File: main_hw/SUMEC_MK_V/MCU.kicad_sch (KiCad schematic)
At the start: 7 parts, among them U3 24CW1280T-I/OT, U4 ESP32-S3-WROOM-1

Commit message: plotting + boms
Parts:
- renumbered U3 to Ue
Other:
- note removed: "CHANGE LABELS"
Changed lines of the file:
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@@
 	(text "GPIO  | NAME      | DESC. \n02    | MAIN_BTN  | Schrack light switch; --debounced --pullup \n05    | R_LED     | LEDs, Indication --debug\n06    | G_LED     | LEDs, Indication --debug\n09    | BUZZER    | Passive buzzer\n10    | MISO      | SPI; SD Card\n11    | CLOCK     | SPI clock; SD Card, MAX7219\n12    | MOSI      | SPI; SD Card, MAX7219\n04    | cSelect0  | Chipselect for MAX7219; --defHigh\n13    | cSelect1  | Chipselect for SD Card; --defHigh\n38    | D_EXT1    | External device, eg: LEDs, Button\n39    | D_EXT2    | External device, eg: LEDs, Button\n40    | D_EXT3    | External device, eg: LEDs, Button\n41    | MODE_SW   | External switch, --unused\n42    | RESET_SW  | External switch, Time/Score reset\n\n"
 		(exclude_from_sim no)
-		(at 135.89 139.7 0)
+		(at 139.065 139.7 0)
 		(effects
 			(font
@@
 			)
 			(justify left bottom)
-		)
-	)
-	(text "CHANGE LABELS"
-		(exclude_from_sim no)
-		(at 171.196 43.18 0)
-		(effects
-			(font
-				(size 1.27 1.27)
-			)
 		)
 	)
@@
 	)
 	(no_connect
-		(at 205.74 71.12)
+		(at 208.28 71.12)
 	)
 	(no_connect
-		(at 205.74 73.66)
+		(at 208.28 73.66)
 	)
 	(no_connect
@@
 	(wire
 		(pts
+			(xy 208.28 73.66) (xy 205.74 73.66)
+		)
+		(stroke
+			(width 0)
+			(type default)
+		)
+	)
+	(wire
+		(pts
 			(xy 186.69 40.64) (xy 186.69 46.99)
 		)
@@
 		(pts
 			(xy 92.71 135.89) (xy 93.98 135.89)
+		)
+		(stroke
+			(width 0)
+			(type default)
+		)
+	)
+	(wire
+		(pts
+			(xy 208.28 71.12) (xy 205.74 71.12)
 		)
 		(stroke
@@
 				(justify right)
 				(hide yes)
-			)
-		)
-	)
-	(netclass_flag ""
-		(length 2.54)
-		(shape round)
-		(at 219.71 139.7 0)
-		(fields_autoplaced yes)
-		(effects
-			(font
-				(size 1.27 1.27)
-			)
-			(justify left bottom)
-		)
-		(property "Netclass" "ARES"
-			(at 220.4085 137.16 0)
-			(effects
-				(font
-					(size 1.27 1.27)
-				)
-				(justify left)
-			)
-		)
-		(property "Component Class" "Resistor"
-			(at 220.4085 138.6205 0)
-			(effects
-				(font
-					(size 1.27 1.27)
-					(italic yes)
-				)
-				(justify left)
 			)
 		)
@@
 			)
 		)
+		(property "Sim.Device" ""
+			(at 190.5 78.74 0)
+			(effects
+				(font
+					(size 1.27 1.27)
+				)
+			)
+		)
+		(property "Sim.Pins" ""
+			(at 190.5 78.74 0)
+			(effects
+				(font
+					(size 1.27 1.27)
+				)
+			)
+		)
+		(property "Sim.Type" ""
+			(at 190.5 78.74 0)
+			(effects
+				(font
+					(size 1.27 1.27)
+				)
+			)
+		)
 		(pin "7"
 		)
@@
 		(dnp no)
 		(fields_autoplaced yes)
-		(property "Reference" "U3"
+		(property "Reference" "Ue"
 			(at 96.1741 137.16 0)
 			(effects
@@
 				)
 				(hide yes)
+			)
+		)
+		(property "Sim.Device" ""
+			(at 93.98 147.32 0)
+			(effects
+				(font
+					(size 1.27 1.27)
+				)
+			)
+		)
+		(property "Sim.Pins" ""
+			(at 93.98 147.32 0)
+			(effects
+				(font
+					(size 1.27 1.27)
+				)
+			)
+		)
+		(property "Sim.Type" ""
+			(at 93.98 147.32 0)
+			(effects
+				(font
+					(size 1.27 1.27)
+				)
 			)
 		)
@@
 			(project "SUMEC_MK_V"
 				(path "/900bd7ac-cdf9-4a2f-8b1f-2c21e3760046/7b93d7c5-db1a-415c-92e4-9ebec6cf195f"
-					(reference "U3")
+					(reference "Ue")
 					(unit 1)
 				)
@@
 				)
 				(hide yes)
+			)
+		)
+		(property "Sim.Device" ""
+			(at 222.25 81.28 0)
+			(effects
+				(font
+					(size 1.27 1.27)
+				)
+			)
+		)
+		(property "Sim.Pins" ""
+			(at 222.25 81.28 0)
+			(effects
+				(font
+					(size 1.27 1.27)
+				)
+			)
+		)
+		(property "Sim.Type" ""
+			(at 222.25 81.28 0)
+			(effects
+				(font
+					(size 1.27 1.27)
+				)
 			)
 		)
@@
 			)
 		)
+		(property "Sim.Device" ""
+			(at 88.9 135.89 0)
+			(effects
+				(font
+					(size 1.27 1.27)
+				)
+			)
+		)
+		(property "Sim.Pins" ""
+			(at 88.9 135.89 0)
+			(effects
+				(font
+					(size 1.27 1.27)
+				)
+			)
+		)
+		(property "Sim.Type" ""
+			(at 88.9 135.89 0)
+			(effects
+				(font
+					(size 1.27 1.27)
+				)
+			)
+		)
 		(pin "1"
 		)
@@
 			)
 		)
+		(property "Sim.Device" ""
+			(at 193.04 40.64 0)
+			(effects
+				(font
+					(size 1.27 1.27)
+				)
+			)
+		)
+		(property "Sim.Pins" ""
+			(at 193.04 40.64 0)
+			(effects
+				(font
+					(size 1.27 1.27)
+				)
+			)
+		)
+		(property "Sim.Type" ""
+			(at 193.04 40.64 0)
+			(effects
+				(font
+					(size 1.27 1.27)
+				)
+			)
+		)
 		(pin "1"
 		)
@@
 				)
 				(hide yes)
+			)
+		)
+		(property "Sim.Device" ""
+			(at 229.87 81.28 0)
+			(effects
+				(font
+					(size 1.27 1.27)
+				)
+			)
+		)
+		(property "Sim.Pins" ""
+			(at 229.87 81.28 0)
+			(effects
+				(font
+					(size 1.27 1.27)
+				)
+			)
+		)
+		(property "Sim.Type" ""
+			(at 229.87 81.28 0)
+			(effects
+				(font
+					(size 1.27 1.27)
+				)
 			)
 		)
@@
 			)
 		)
+		(property "Sim.Device" ""
+			(at 193.04 46.99 0)
+			(effects
+				(font
+					(size 1.27 1.27)
+				)
+			)
+		)
+		(property "Sim.Pins" ""
+			(at 193.04 46.99 0)
+			(effects
+				(font
+					(size 1.27 1.27)
+				)
+			)
+		)
+		(property "Sim.Type" ""
+			(at 193.04 46.99 0)
+			(effects
+				(font
+					(size 1.27 1.27)
+				)
+			)
+		)

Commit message: 67yfhtgftu
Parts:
- renumbered Ue to U3
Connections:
- net EN_L: now also U4.7 (IO7); no longer U4.12 (IO8)
- net EN_R: now also U4.12 (IO8); no longer U4.7 (IO7)
- net PH_L: now also U4.6 (IO6); no longer U4.11 (IO18)
- net PH_R: now also U4.11 (IO18); no longer U4.6 (IO6)
- net SHARP_L: now also U4.31 (IO38); no longer U4.18 (IO10)
- net SHARP_R: now also U4.18 (IO10); no longer U4.31 (IO38)
- net BZ_PWM renamed BZ_IO02
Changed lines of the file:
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@@
 		)
 	)
-	(global_label "SHARP_R"
+	(global_label "SHARP_L"
 		(shape input)
 		(at 205.74 81.28 0)
@@
 		)
 		(property "Intersheetrefs" "${INTERSHEET_REFS}"
-			(at 213.9109 81.28 0)
+			(at 213.8005 81.28 0)
 			(effects
 				(font
@@
 		)
 	)
-	(global_label "EN_R"
+	(global_label "EN_L"
 		(shape output)
 		(at 167.64 78.74 180)
@@
 		)
 		(property "Intersheetrefs" "${INTERSHEET_REFS}"
-			(at 162.1264 78.74 0)
-			(effects
-				(font
-					(size 1.27 1.27)
-				)
-				(justify right)
-				(hide yes)
-			)
-		)
-	)
-	(global_label "BZ_PWM"
+			(at 162.2368 78.74 0)
+			(effects
+				(font
+					(size 1.27 1.27)
+				)
+				(justify right)
+				(hide yes)
+			)
+		)
+	)
+	(global_label "BZ_IO02"
 		(shape output)
 		(at 166.37 66.04 180)
@@
 		)
 		(property "Intersheetrefs" "${INTERSHEET_REFS}"
-			(at 158.7667 66.04 0)
+			(at 159.1643 66.04 0)
 			(effects
 				(font
@@
 		)
 	)
-	(global_label "PH_R"
+	(global_label "PH_L"
 		(shape output)
 		(at 167.64 76.2 180)
@@
 		)
 		(property "Intersheetrefs" "${INTERSHEET_REFS}"
-			(at 162.1352 76.2 0)
+			(at 162.2456 76.2 0)
 			(effects
 				(font
@@
 		)
 	)
-	(global_label "SHARP_L"
+	(global_label "SHARP_R"
 		(shape input)
 		(at 167.64 86.36 180)
@@
 		)
 		(property "Intersheetrefs" "${INTERSHEET_REFS}"
-			(at 159.5795 86.36 0)
+			(at 159.4691 86.36 0)
 			(effects
 				(font
@@
 		)
 	)
-	(global_label "PH_L"
+	(global_label "PH_R"
 		(shape output)
 		(at 205.74 63.5 0)
@@
 		)
 		(property "Intersheetrefs" "${INTERSHEET_REFS}"
-			(at 211.1344 63.5 0)
+			(at 211.2448 63.5 0)
 			(effects
 				(font
@@
 		)
 	)
-	(global_label "EN_L"
+	(global_label "EN_R"
 		(shape output)
 		(at 167.64 81.28 180)
@@
 		)
 		(property "Intersheetrefs" "${INTERSHEET_REFS}"
-			(at 162.2368 81.28 0)
+			(at 162.1264 81.28 0)
 			(effects
 				(font
@@
 		(dnp no)
 		(fields_autoplaced yes)
-		(property "Reference" "Ue"
-			(at 96.1741 137.16 0)
+		(property "Reference" "U3"
+			(at 96.1233 137.16 0)
 			(effects
 				(font
@@
 		)
 		(property "Value" "24CW1280T-I/OT"
-			(at 96.1741 139.7 0)
+			(at 96.1233 139.7 0)
 			(effects
 				(font
@@
 			(project "SUMEC_MK_V"
 				(path "/900bd7ac-cdf9-4a2f-8b1f-2c21e3760046/7b93d7c5-db1a-415c-92e4-9ebec6cf195f"
-					(reference "Ue")
+					(reference "U3")
 					(unit 1)
 				)

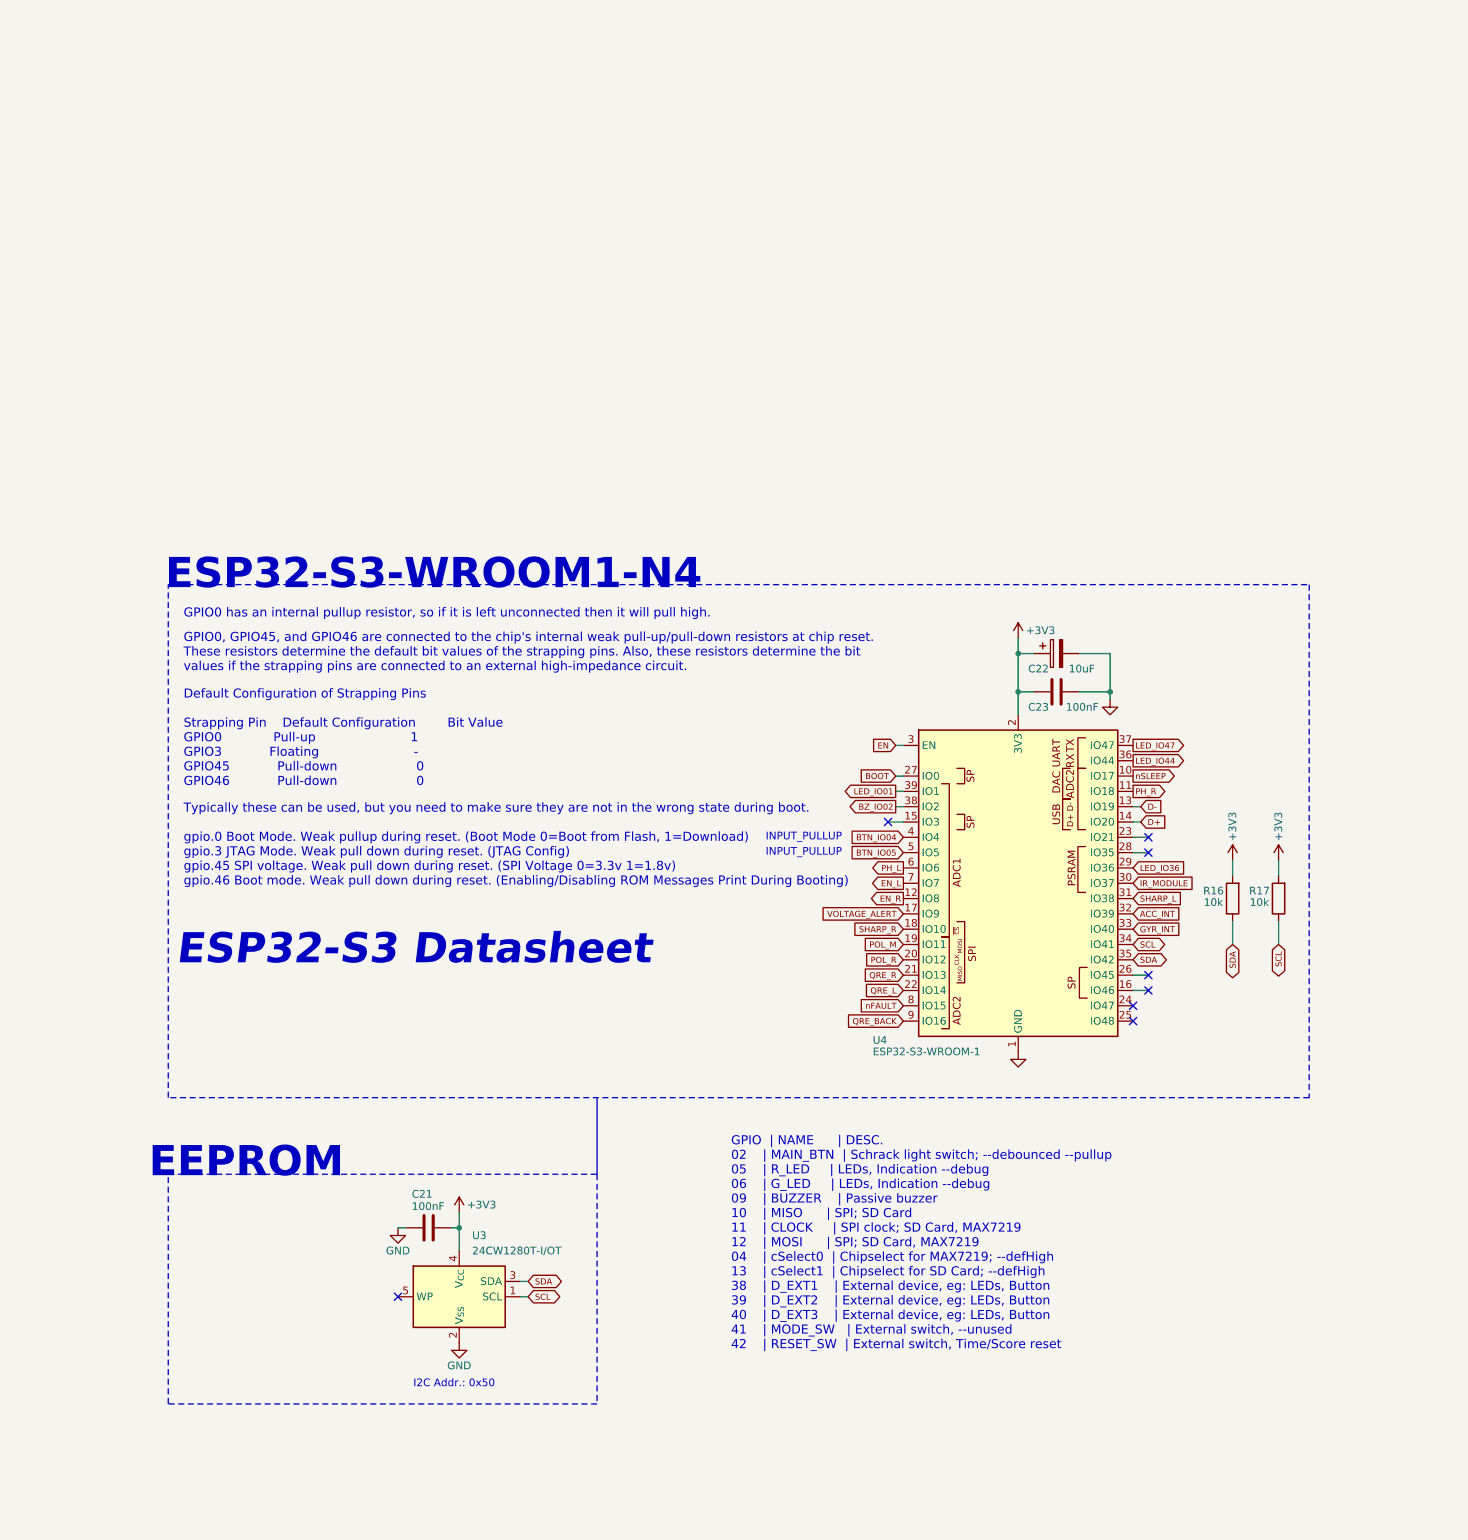
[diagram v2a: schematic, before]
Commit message: MK5 bugfix fixed POL_L, minor changes, deleted nSLEEP and nFault connections to the MCU
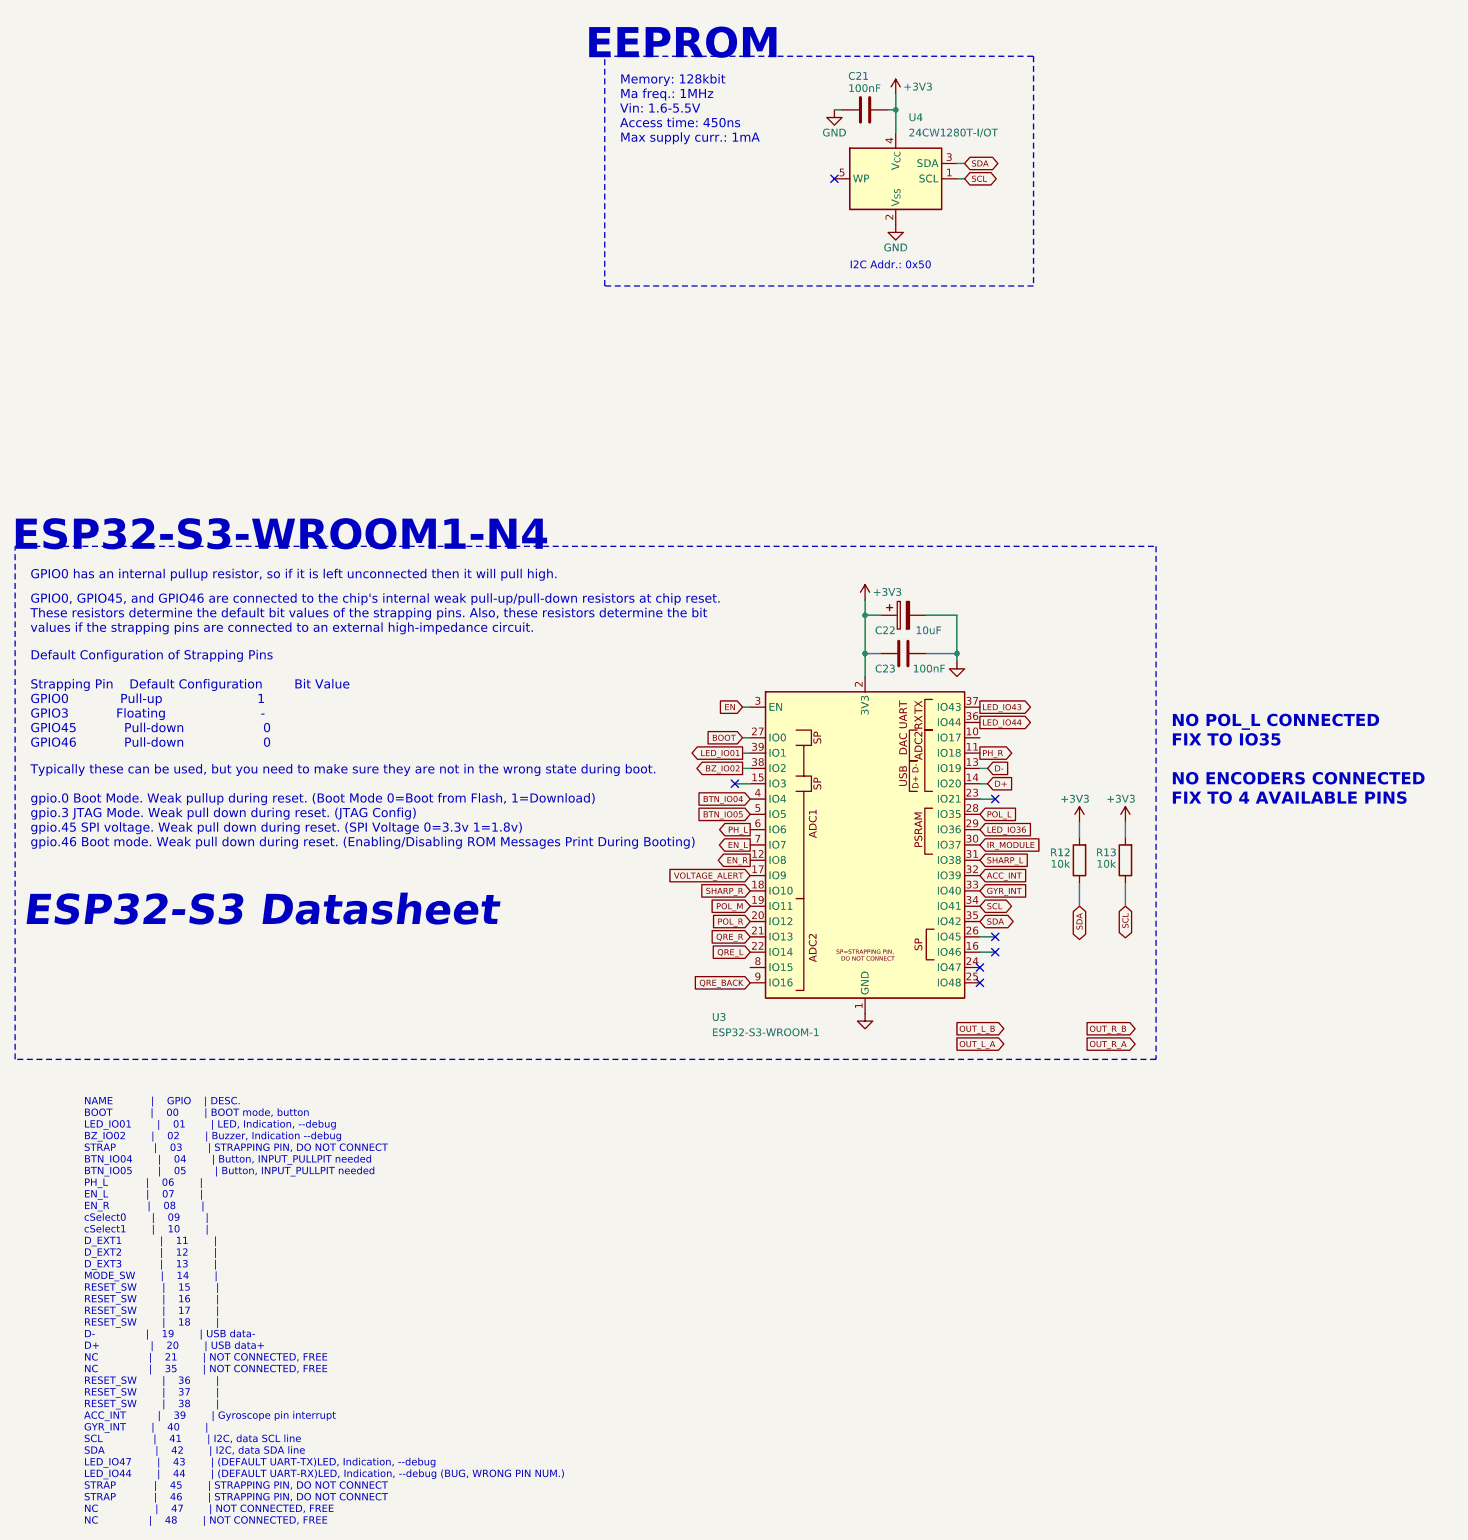
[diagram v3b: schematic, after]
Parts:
- removed U4: ESP32-S3-WROOM-1, PCM_Espressif:ESP32-S3-WROOM-1, symbol sumec_sch_lib:ESP32-S3-WROOM-1_CUSTOM_made_by_bismarx
- added U3: ESP32-S3-WROOM-1, PCM_Espressif:ESP32-S3-WROOM-1, symbol sumec_sch_lib:ESP32-S3-WROOM-1_CUSTOM_made_by_bismarx
- renumbered R16 to R12, R17 to R13, U3 to U4
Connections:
- net +3V3: now also U3.2 (3V3)
- net ACC_INT: now also U3.32 (IO39)
- net BOOT: now also U3.27 (IO0)
- net BTN_IO04: now also U3.4 (IO4)
- net BTN_IO05: now also U3.5 (IO5)
- net BZ_IO02: now also U3.38 (IO2)
- net D+: now also U3.14 (IO20)
- net D-: now also U3.13 (IO19)
- net EN: now also U3.3 (EN)
- net EN_L: now also U3.7 (IO7)
- net EN_R: now also U3.12 (IO8)
- net GND: now also U3.1 (GND), U3.40 (GND), U3.41 (GND)
- net GYR_INT: now also U3.33 (IO40)
- net IR_MODULE: now also U3.30 (IO37)
- net LED_IO01: now also U3.39 (IO1)
- net LED_IO36: now also U3.29 (IO36)
- net LED_IO44: now also U3.36 (IO44)
- net PH_L: now also U3.6 (IO6)
- net PH_R: now also U3.11 (IO18)
- net POL_M: now also U3.19 (IO11)
- net POL_R: now also U3.20 (IO12)
- net QRE_BACK: now also U3.9 (IO16)
- net QRE_L: now also U3.22 (IO14)
- net QRE_R: now also U3.21 (IO13)
- net SCL: now also U3.34 (IO41)
- net SDA: now also U3.35 (IO42)
- net SHARP_L: now also U3.31 (IO38)
- net SHARP_R: now also U3.18 (IO10)
- net VOLTAGE_ALERT: now also U3.17 (IO9)
- new net LED_IO43: U3.37 (IO43)
- new net POL_L: U3.28 (IO35)
- no-connect marks 8 -> 7
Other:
- note added: "Memory: 128kbit Ma freq.: 1MHz Vin: 1.6-5.5V Access time: 450ns Max supply curr.: 1mA"
- note added: "NAME | GPIO | DESC. BOOT | 00 | BOOT mode, button LED_IO01 | 01 | LED, Indication, --debug BZ_IO02 | 02 | Buzzer, Indication --debug STRAP | 03 | STRAPPING PIN, DO NOT CONNECT BTN_IO04 | 04 | Button, INPUT_PULLPIT needed BTN_IO05 | 05 | Button, INPUT_PULLPIT needed PH_L | 06 | EN_L | 07 | EN_R | 08 | cSelect0 | 09 | cSelect1 | 10 | D_EXT1 | 11 | D_EXT2 | 12 | D_EXT3 | 13 | MODE_SW | 14 | RESET_SW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"
- note added: "NO POL_L CONNECTED FIX TO IO35 NO ENCODERS CONNECTED FIX TO 4 AVAILABLE PINS"
- note removed: "GPIO | NAME | DESC. 02 | MAIN_BTN | Schrack light switch; --debounced --pullup 05 | R_LED | LEDs, Indication --debug 06 | G_LED | LEDs, Indication --debug 09 | BUZZER | Passive buzzer 10 | MISO | SPI; SD Card 11 | CLOCK | SPI clock; SD Card, MAX7219 12 | MOSI | SPI; SD Card, MAX7219 04 | cSelect0 | Chipselect for MAX7219; --defHigh 13 | cSelect1 | Chipselect for SD Card; --defHigh 38 | D_EXT1 | E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"
- note removed: "INPUT_PULLUP"
- moved on the sheet: C21, C22, C23, R12, R13, U4

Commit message: MK5 changes and deletion of useless files
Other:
- note added: "BAD PINOUT"
- note added: "SOME PINS ARE NOT CONNECTED IN SCHEMATIC"
- moved on the sheet: C21, C22, C23, R12, R13, U3, U4

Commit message: schematic fixes
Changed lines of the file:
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@@
 	(global_label "OUT_R_B"
 		(shape output)
-		(at 219.71 113.03 0)
-		(fields_autoplaced yes)
-		(effects
-			(font
-				(face "Bahnschrift")
-				(size 1 1)
-				(color 0 0 0 1)
-			)
-			(justify left)
-		)
-		(property "Intersheetrefs" "${INTERSHEET_REFS}"
-			(at 227.3876 113.03 0)
+		(at 256.54 71.12 0)
+		(fields_autoplaced yes)
+		(effects
+			(font
+				(face "Bahnschrift")
+				(size 1 1)
+				(color 0 0 0 1)
+			)
+			(justify left)
+		)
+		(property "Intersheetrefs" "${INTERSHEET_REFS}"
+			(at 264.2176 71.12 0)
 			(effects
 				(font
@@
 	(global_label "OUT_R_A"
 		(shape output)
-		(at 219.71 115.57 0)
-		(fields_autoplaced yes)
-		(effects
-			(font
-				(face "Bahnschrift")
-				(size 1 1)
-				(color 0 0 0 1)
-			)
-			(justify left)
-		)
-		(property "Intersheetrefs" "${INTERSHEET_REFS}"
-			(at 227.3895 115.57 0)
+		(at 256.54 73.66 0)
+		(fields_autoplaced yes)
+		(effects
+			(font
+				(face "Bahnschrift")
+				(size 1 1)
+				(color 0 0 0 1)
+			)
+			(justify left)
+		)
+		(property "Intersheetrefs" "${INTERSHEET_REFS}"
+			(at 264.2195 73.66 0)
 			(effects
 				(font
@@
 	(global_label "OUT_L_A"
 		(shape output)
-		(at 198.12 115.57 0)
-		(fields_autoplaced yes)
-		(effects
-			(font
-				(face "Bahnschrift")
-				(size 1 1)
-				(color 0 0 0 1)
-			)
-			(justify left)
-		)
-		(property "Intersheetrefs" "${INTERSHEET_REFS}"
-			(at 205.6891 115.57 0)
+		(at 234.95 73.66 0)
+		(fields_autoplaced yes)
+		(effects
+			(font
+				(face "Bahnschrift")
+				(size 1 1)
+				(color 0 0 0 1)
+			)
+			(justify left)
+		)
+		(property "Intersheetrefs" "${INTERSHEET_REFS}"
+			(at 242.5191 73.66 0)
 			(effects
 				(font
@@
 	(global_label "OUT_L_B"
 		(shape output)
-		(at 198.12 113.03 0)
-		(fields_autoplaced yes)
-		(effects
-			(font
-				(face "Bahnschrift")
-				(size 1 1)
-				(color 0 0 0 1)
-			)
-			(justify left)
-		)
-		(property "Intersheetrefs" "${INTERSHEET_REFS}"
-			(at 205.6872 113.03 0)
-			(effects
-				(font
+		(at 234.95 71.12 0)
+		(fields_autoplaced yes)
+		(effects
+			(font
+				(face "Bahnschrift")
+				(size 1 1)
+				(color 0 0 0 1)
+			)
+			(justify left)
+		)
+		(property "Intersheetrefs" "${INTERSHEET_REFS}"
+			(at 242.5172 71.12 0)
+			(effects
+				(font
